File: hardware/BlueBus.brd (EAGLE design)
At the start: 90 x 60 mm, 130 parts, among them Q1 NMOSFET-BSS138K, Q2 PMOSFET-DMP1045UQ, Q3 NMOSFET-BSS138K, X1 CRYSTAL-12MHZ

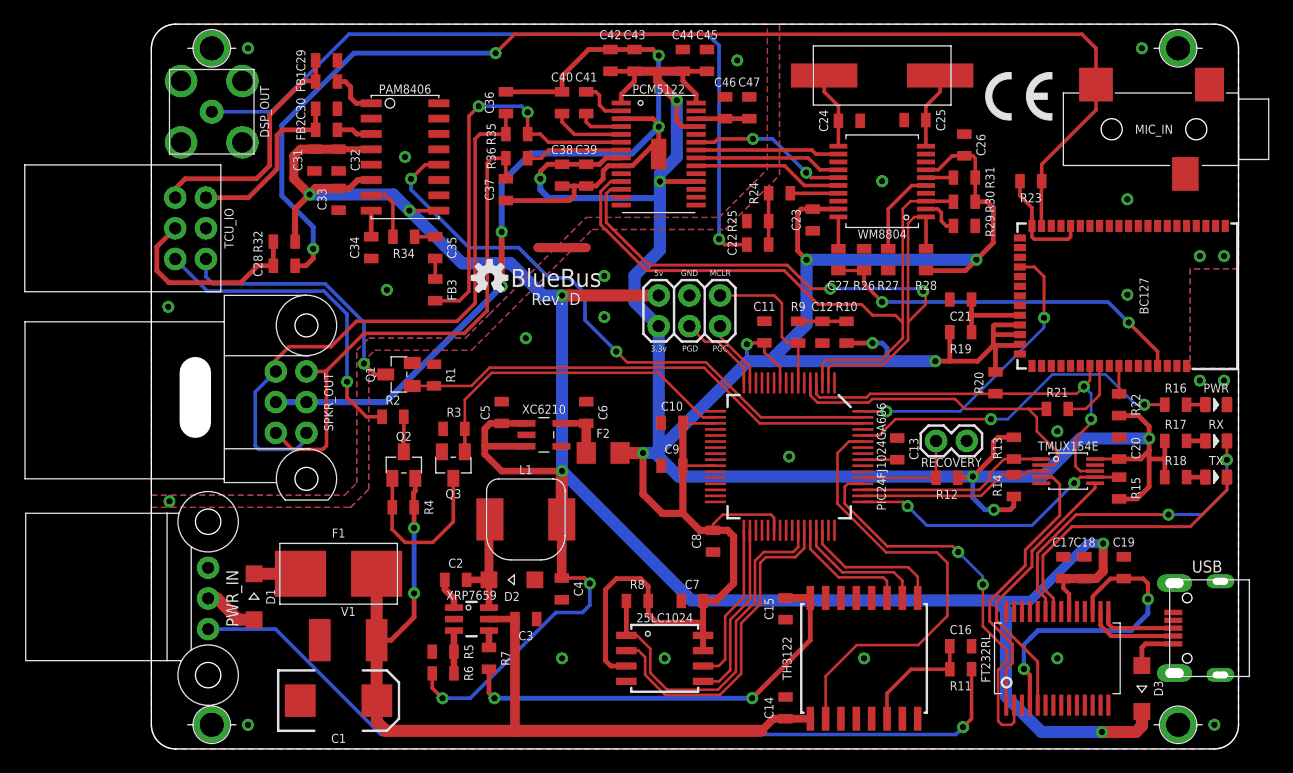
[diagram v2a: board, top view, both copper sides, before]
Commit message: [IMP] hardware: Production V1 * Add Fiducials * Fix bugs with PCM5122 DGND being floating and VCOM not being tied to AGND * Adjust routing so that all traces intersect at 90 degree angles on different layers * Adjust traces to not follow the same track on different sides of the board * Add additional ground stiches * Improve placement of decoupling caps for superior ground returns
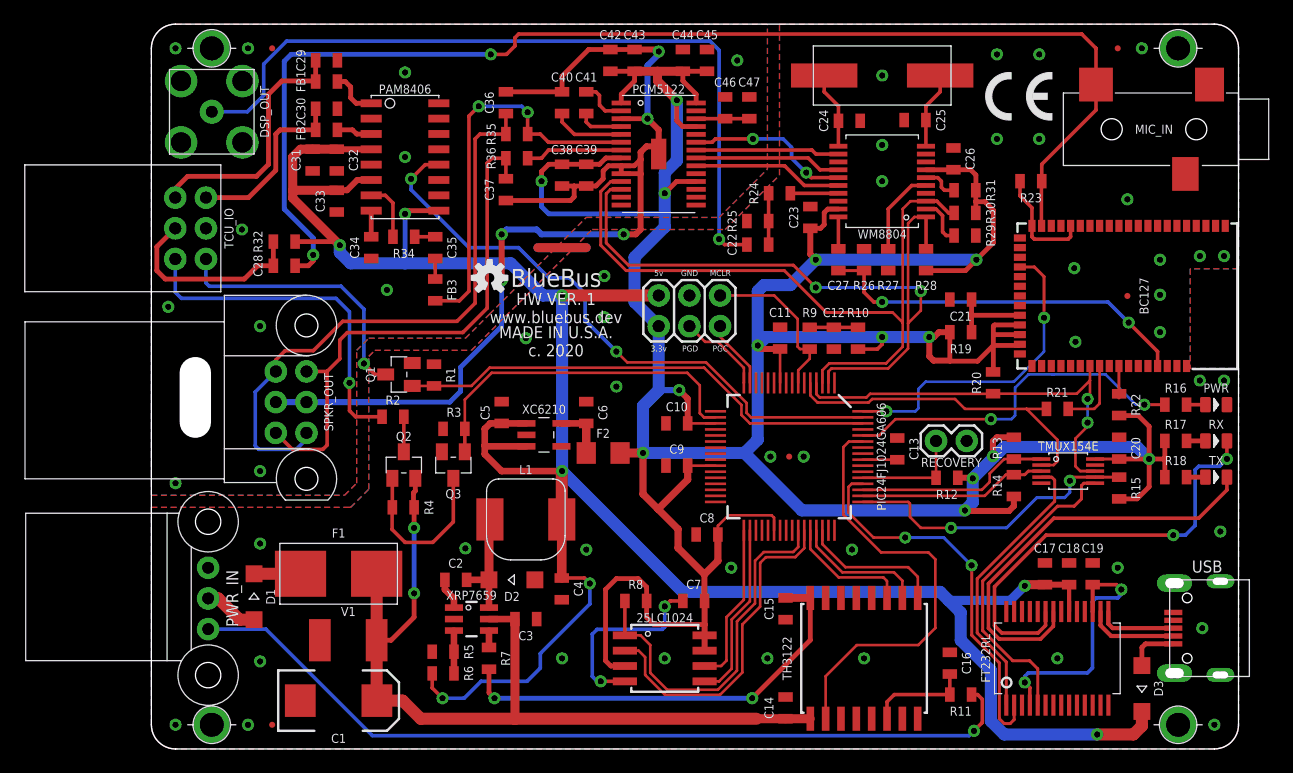
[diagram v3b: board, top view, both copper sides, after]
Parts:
- added FID1, FID2, FID3, FID4, FID5: FIDUCIAL_0.5MM, MF_Aesthetics:FIDUCIAL_0.5MM
- 25LC1024: device ICs:SOIC-8 -> ICs:SOIJ-8
- moved C19 2.62 mm to (77.9, 14.5)
- moved R11 2.10 mm to (67.0, 4.50)
- moved C16 1.66 mm to (66.1, 7.10), turned to 90 degrees
- moved C17 1.60 mm to (74.0, 14.5)
- moved C26 1.46 mm to (66.4, 48.9)
- moved C11 1.39 mm to (52.0, 34.0)
- moved C18 1.37 mm to (76.0, 14.5)
- moved C12 1.07 mm to (56.5, 34.0)
- moved R10 1.07 mm to (58.5, 34.0)
- moved R9 1.07 mm to (54.5, 34.0)
- moved R31 1.05 mm to (67.3, 46.2)
- moved R30 0.93 mm to (67.3, 44.4)
- moved R29 0.80 mm to (67.3, 42.5)
- moved C8 0.74 mm to (46.0, 17.8), turned to 0 degrees
- moved C10 0.40 mm to (43.5, 26.9)
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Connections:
- new net 12V_VIN: D1.A, PWR_IN.2
- new net BT_URX_RES: BC127.42, R21.2
- new net RAW_3.3V: C6.1, F2.1, XC6210.5
- new net VIN_DIODE: D1.C, F1.IN
- net 3.3V: no longer C6.1, F2.1, XC6210.5
- net AGND: now also PCM5122.10
- net BT_URX: no longer BC127.42, R21.2
- net GND: now also PCM5122.27
- net VIN: no longer D1.A, D1.C, F1.IN, PWR_IN.2
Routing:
- net GND: track 8.00 -> 24.2 mm, vias 25 -> 52
- net TX_LED: track 23.5 -> 35.1 mm
- net VIN: track 84.2 -> 72.9 mm
- net RX_LED: track 27.0 -> 36.9 mm
- net 3.3V: track 326.9 -> 319.4 mm, vias 12 -> 14
- net BT_URX_RES: track 0.00 -> 5.89 mm
- net BT_URX: track 33.6 -> 28.1 mm
- net 12V_VIN: track 0.00 -> 4.53 mm
- net RAW_3.3V: track 0.00 -> 4.50 mm
- net AGND: track 88.6 -> 92.6 mm, vias 4 -> 5
- net SYS_3V3: track 25.6 -> 21.8 mm
- net VIN_DIODE: track 0.00 -> 3.85 mm
- net BT_MIC_L: track 102.0 -> 105.3 mm
- net SYS_URX: track 23.2 -> 26.3 mm
- net TEL_ON_IO: track 26.6 -> 28.9 mm
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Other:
- board text added: "468"
- board text added: "HW VER. 1"
- board text added: "MADE IN U.S.A."
- board text added: "c. 2020"
- board text added: "www.bluebus.dev"
- board text removed: "497"
- board text removed: "Rev. D"

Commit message: [IMP] hardware: Production V1 * Fix issue with silkscreen names * Add ground VIA
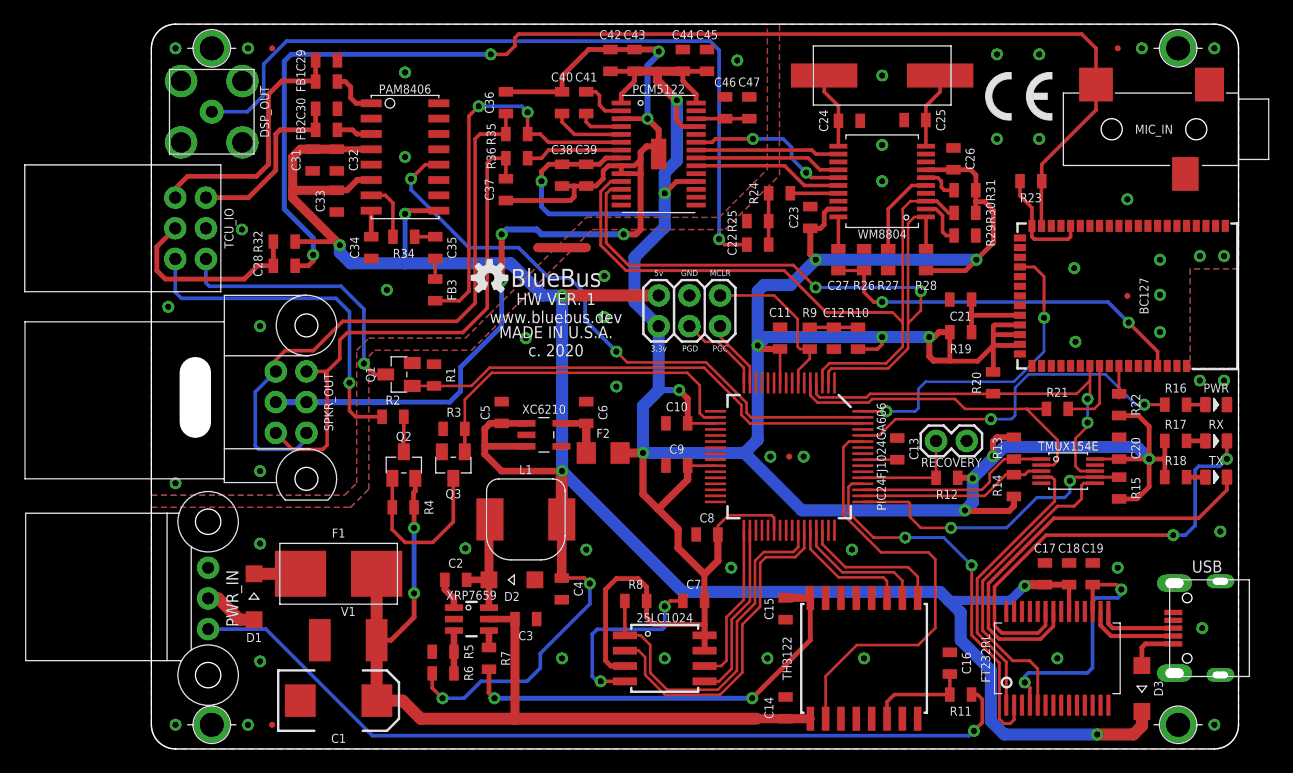
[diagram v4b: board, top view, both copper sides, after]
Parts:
- R28, R30: value 10k -> 4.7k
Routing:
- net GND: vias 52 -> 53
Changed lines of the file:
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@@
 <element name="D1" library="Passives" package="SOD123" value="2A/100V" x="8.5" y="12.6" smashed="yes" rot="R270">
 <attribute name="MFG" value="STMicroelectronics" x="-46.11" y="-67.41" size="1.778" layer="27" rot="R270" display="off"/>
-<attribute name="NAME" x="9.5" y="12.6" size="0.75" layer="25" font="vector" ratio="15" rot="R270" align="bottom-center"/>
+<attribute name="NAME" x="8.5" y="9.6" size="0.75" layer="25" font="vector" ratio="15" rot="R180" align="bottom-center"/>
 <attribute name="PN" value="STPS2H100ZFY" x="-46.11" y="-67.41" size="1.778" layer="27" rot="R270" display="off"/>
 <attribute name="VALUE" x="7.5" y="12.6" size="0.5" layer="27" font="vector" ratio="15" rot="R270" align="top-center"/>
@@
 <attribute name="VALUE" x="67.35" y="47.25" size="0.5" layer="27" font="vector" ratio="15" rot="R180" align="top-center"/>
 </element>
-<element name="R28" library="Passives" package="0805" value="10k" x="64.13" y="40.5" smashed="yes" rot="R90">
-<attribute name="DEVICE" value="10KOHM-0805-1/8-1%" x="64.13" y="40.5" size="1.778" layer="27" rot="R90" display="off"/>
+<element name="R28" library="Passives" package="0805" value="4.7k" x="64.13" y="40.5" smashed="yes" rot="R90">
+<attribute name="DEVICE" value="4.7kOHM-0805-1/8-1%" x="64.13" y="40.5" size="1.778" layer="27" rot="R90" display="off"/>
 <attribute name="MFG" value="Panasonic" x="64.13" y="40.5" size="1.778" layer="27" rot="R90" display="off"/>
 <attribute name="NAME" x="64.13" y="38.75" size="0.75" layer="25" font="vector" ratio="15" align="top-center"/>
 <attribute name="PACKAGE" value="0805" x="64.13" y="40.5" size="1.778" layer="27" rot="R90" display="off"/>
-<attribute name="PN" value="ERJ-6ENF1002V" x="64.13" y="40.5" size="1.778" layer="27" rot="R90" display="off"/>
-<attribute name="VALUE" x="65.13" y="40.5" size="0.5" layer="27" font="vector" ratio="15" rot="R90" align="top-center"/>
+<attribute name="PN" value="ERJ-6ENF4701V" x="64.13" y="40.5" size="1.778" layer="27" rot="R90" display="off"/>
+<attribute name="VALUE" value="4.7k" x="65.13" y="40.5" size="0.5" layer="27" font="vector" ratio="15" rot="R90" align="top-center"/>
 </element>
 <element name="R27" library="Passives" package="0805" value="10k" x="61" y="40.5" smashed="yes" rot="R90">
@@
 <attribute name="VALUE" x="62" y="40.5" size="0.5" layer="27" font="vector" ratio="15" rot="R90" align="top-center"/>
 </element>
-<element name="R30" library="Passives" package="0805" value="10k" x="67.35" y="44.375" smashed="yes" rot="R180">
-<attribute name="DEVICE" value="10KOHM-0805-1/8-1%" x="67.35" y="44.375" size="1.778" layer="27" rot="R180" display="off"/>
+<element name="R30" library="Passives" package="0805" value="4.7k" x="67.35" y="44.375" smashed="yes" rot="R180">
+<attribute name="DEVICE" value="4.7kOHM-0805-1/8-1%" x="67.35" y="44.375" size="1.778" layer="27" rot="R180" display="off"/>
 <attribute name="MFG" value="Panasonic" x="67.35" y="44.375" size="1.778" layer="27" rot="R180" display="off"/>
 <attribute name="NAME" x="69.1" y="44.375" size="0.75" layer="25" font="vector" ratio="15" rot="R90" align="top-center"/>
 <attribute name="PACKAGE" value="0805" x="67.35" y="44.375" size="1.778" layer="27" rot="R180" display="off"/>
-<attribute name="PN" value="ERJ-6ENF1002V" x="67.35" y="44.375" size="1.778" layer="27" rot="R180" display="off"/>
-<attribute name="VALUE" x="67.35" y="45.375" size="0.5" layer="27" font="vector" ratio="15" rot="R180" align="top-center"/>
+<attribute name="PN" value="ERJ-6ENF4701V" x="67.35" y="44.375" size="1.778" layer="27" rot="R180" display="off"/>
+<attribute name="VALUE" value="4.7k" x="67.35" y="45.375" size="0.5" layer="27" font="vector" ratio="15" rot="R180" align="top-center"/>
 </element>
 <element name="R25" library="Passives" package="0805" value="110" x="50.2" y="43.7" smashed="yes">
@@
 <contactref element="C44" pad="2"/>
 <via x="48" y="15" extent="1-16" drill="0.51"/>
+<via x="88" y="58" extent="1-16" drill="0.51"/>
 </signal>
 <signal name="VIN" class="3">

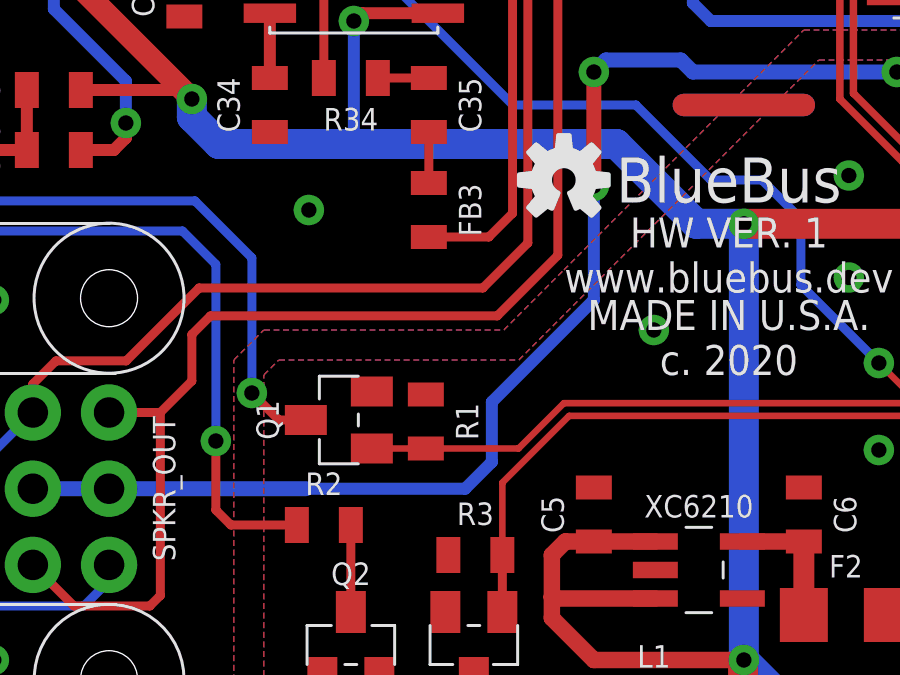
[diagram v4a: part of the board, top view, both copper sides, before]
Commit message: [IMP] hardware: Add via to create ground pour * Add VIA to area without a GND pour * Alter AGND routing slightly
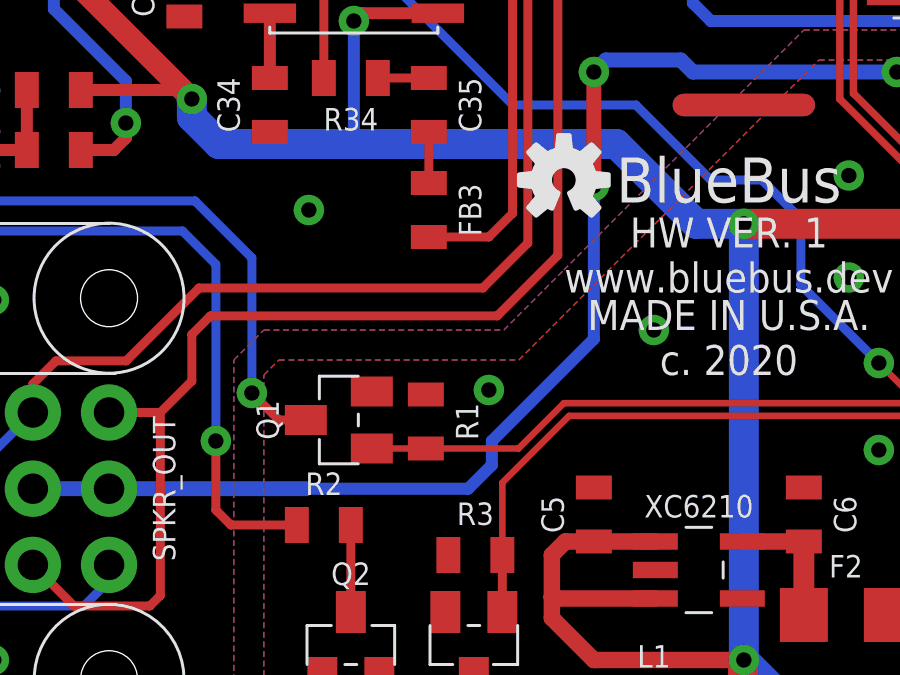
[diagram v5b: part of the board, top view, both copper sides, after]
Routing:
- net GND: vias 53 -> 54
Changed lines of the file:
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@@
 <via x="48" y="15" extent="1-16" drill="0.51"/>
 <via x="88" y="58" extent="1-16" drill="0.51"/>
+<via x="25.5" y="32" extent="1-16" drill="0.51"/>
 </signal>
 <signal name="VIN" class="3">
@@
 <wire x1="34" y1="55.7" x2="36.2" y2="57.9" width="0.4" layer="1"/>
 <wire x1="36.2" y1="57.9" x2="38" y2="57.9" width="0.4" layer="1"/>
-<wire x1="19.41" y1="28.71" x2="24.71" y2="28.71" width="0.4" layer="16"/>
-<wire x1="25.6" y1="29.6" x2="25.6" y2="31.6" width="0.4" layer="16"/>
-<wire x1="25.6" y1="31.6" x2="29" y2="35" width="0.4" layer="16"/>
-<wire x1="29" y1="35" x2="29" y2="38.8" width="0.4" layer="16"/>
-<wire x1="24.71" y1="28.71" x2="25.6" y2="29.6" width="0.4" layer="16"/>
+<wire x1="19.41" y1="28.71" x2="24.81" y2="28.71" width="0.4" layer="16"/>
+<wire x1="25.6" y1="29.5" x2="25.6" y2="30.3" width="0.4" layer="16"/>
+<wire x1="25.6" y1="30.3" x2="29" y2="33.7" width="0.4" layer="16"/>
+<wire x1="29" y1="33.7" x2="29" y2="38.8" width="0.4" layer="16"/>
+<wire x1="24.81" y1="28.71" x2="25.6" y2="29.5" width="0.4" layer="16"/>
 <wire x1="29.35" y1="45.4" x2="34.7" y2="45.4" width="0.4" layer="1"/>
 <wire x1="34.7" y1="45.4" x2="35" y2="45.7" width="0.4" layer="1"/>
